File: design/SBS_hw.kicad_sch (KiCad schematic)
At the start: 32 parts

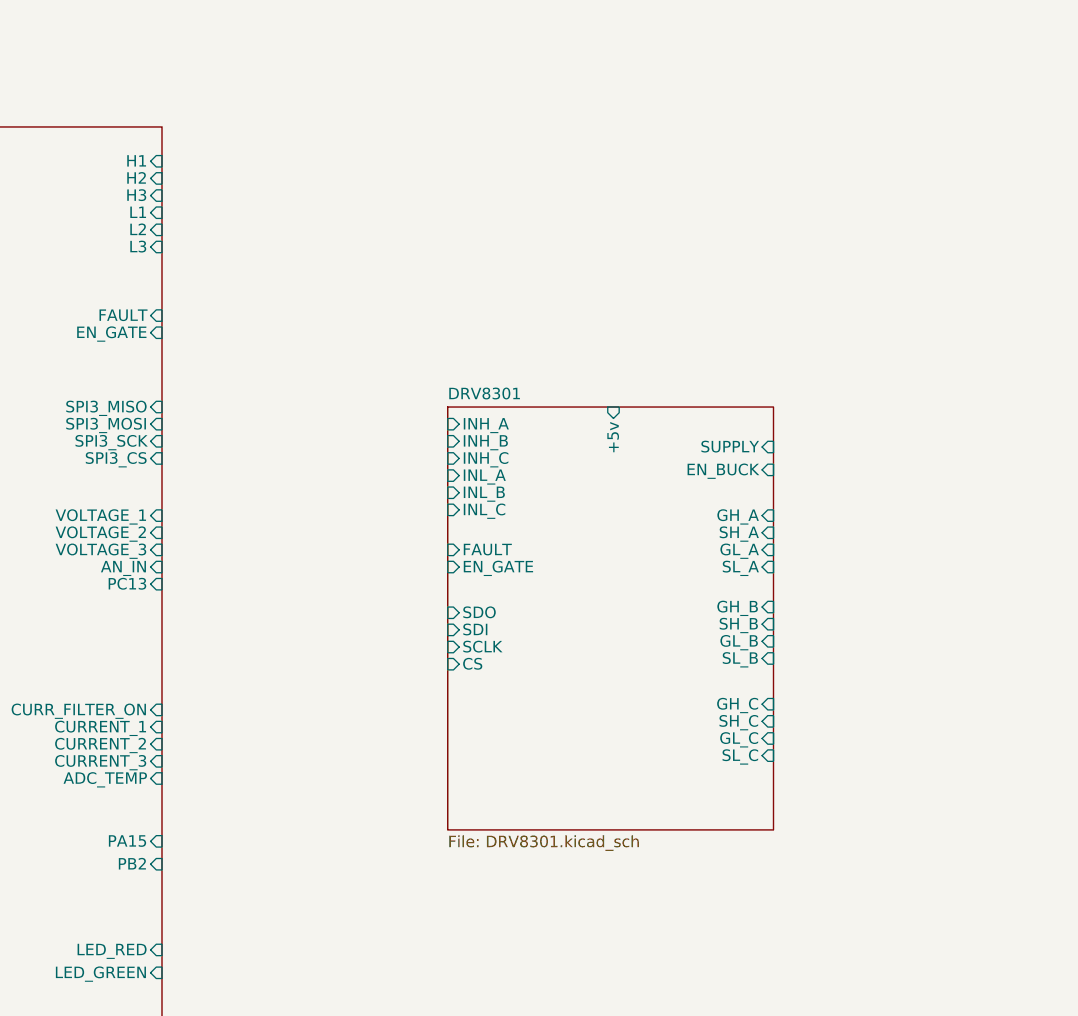
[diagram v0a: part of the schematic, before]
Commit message: add documentation, manufacturing outputs, and Power sheet WIP
- Add requirements.md, schematic_review.md, battery_design.md,
  onewheel_system_design.md, vesc_firmware_notes.md
- Add manufacturing/BOM.md (LCSC parts with costs) and schematic PDF
- Add design/Power.kicad_sch (Phase A half-bridge WIP)
- Update DRV8301, top-level and project KiCad files
- Remove old 2023 backups and accidentally committed linkedin image

Co-Authored-By: Claude Sonnet 4.6 <noreply@anthropic.com>
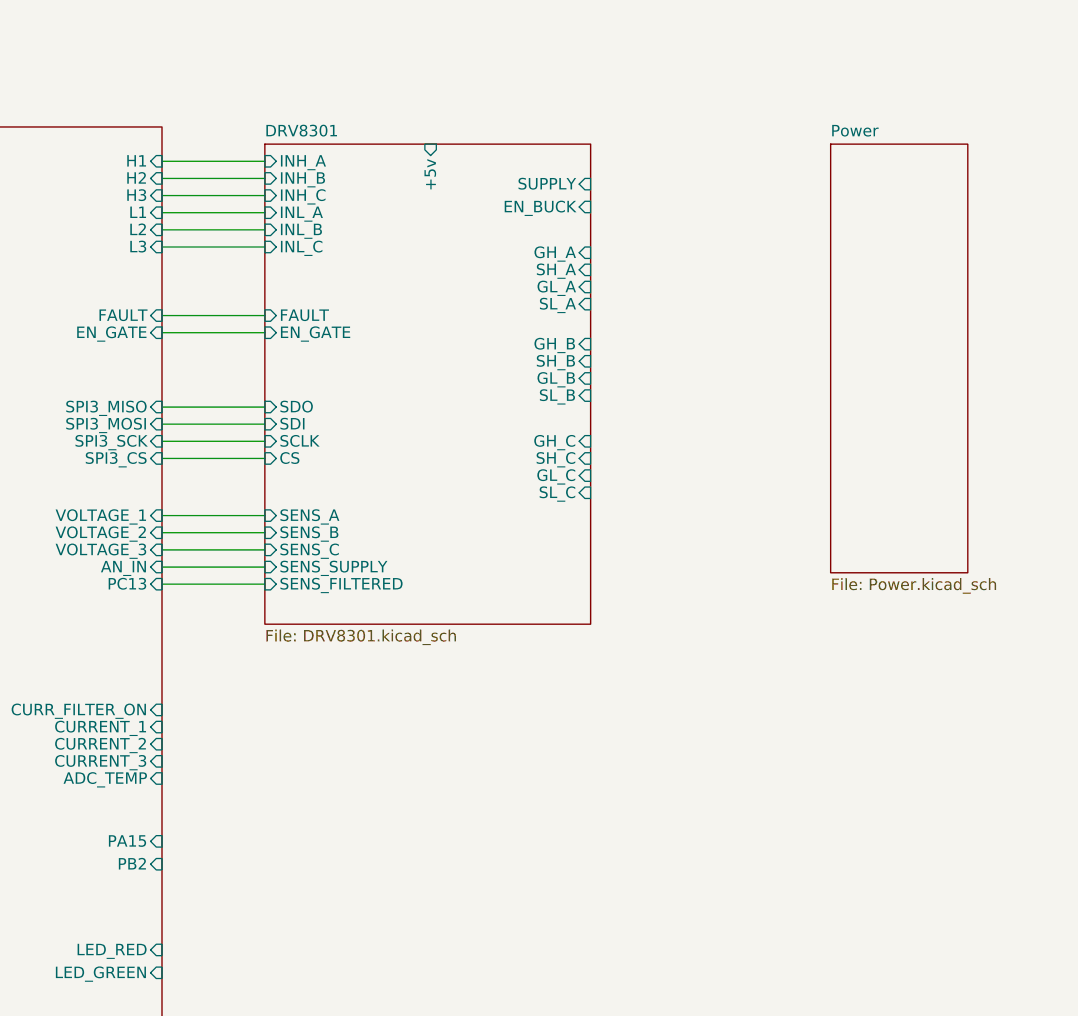
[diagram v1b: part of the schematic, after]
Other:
- added sheet Power (Power.kicad_sch)
- sheet DRV8301 ports: added SENS_A, SENS_B, SENS_C, SENS_FILTERED, SENS_SUPPLY; removed none
